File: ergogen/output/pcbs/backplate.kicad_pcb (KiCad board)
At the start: 2 copper layers, 133.8 x 91.7 mm, 5 parts

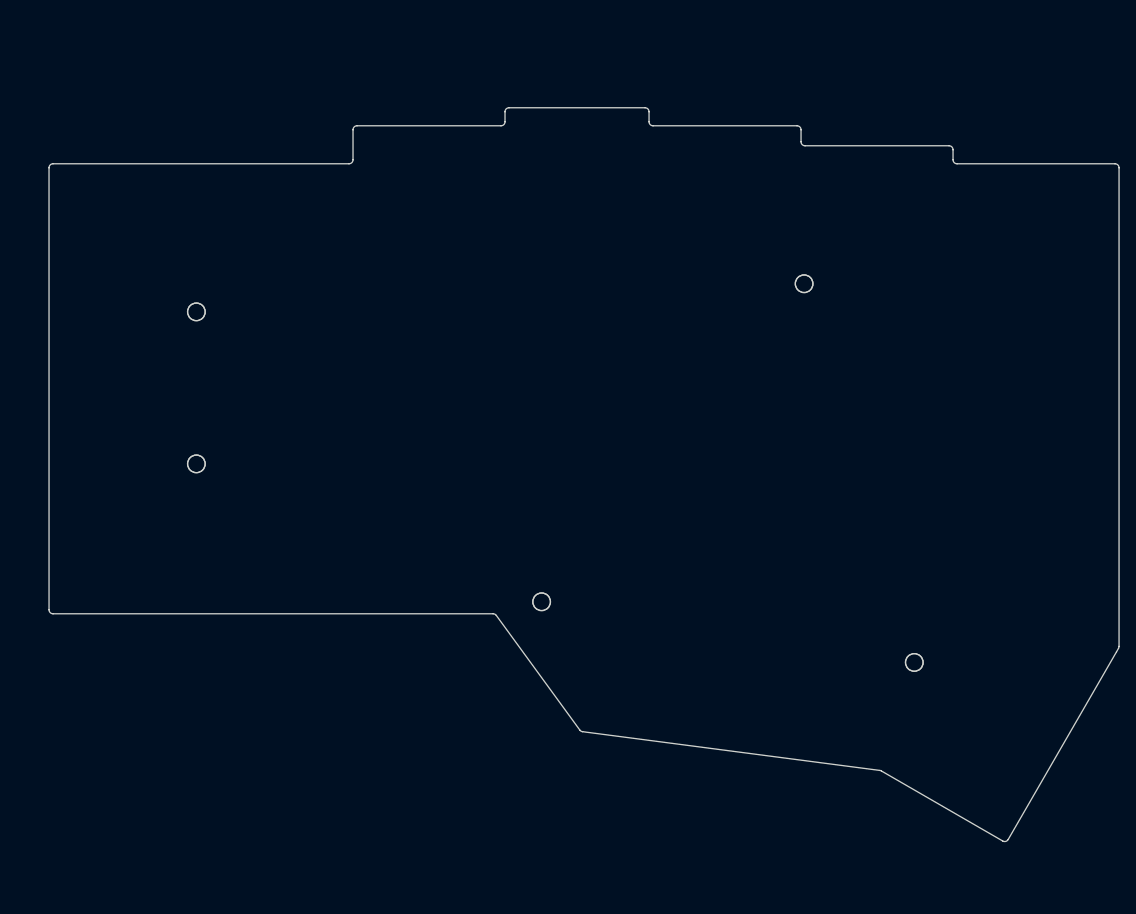
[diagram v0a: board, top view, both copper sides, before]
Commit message: Removed outer column
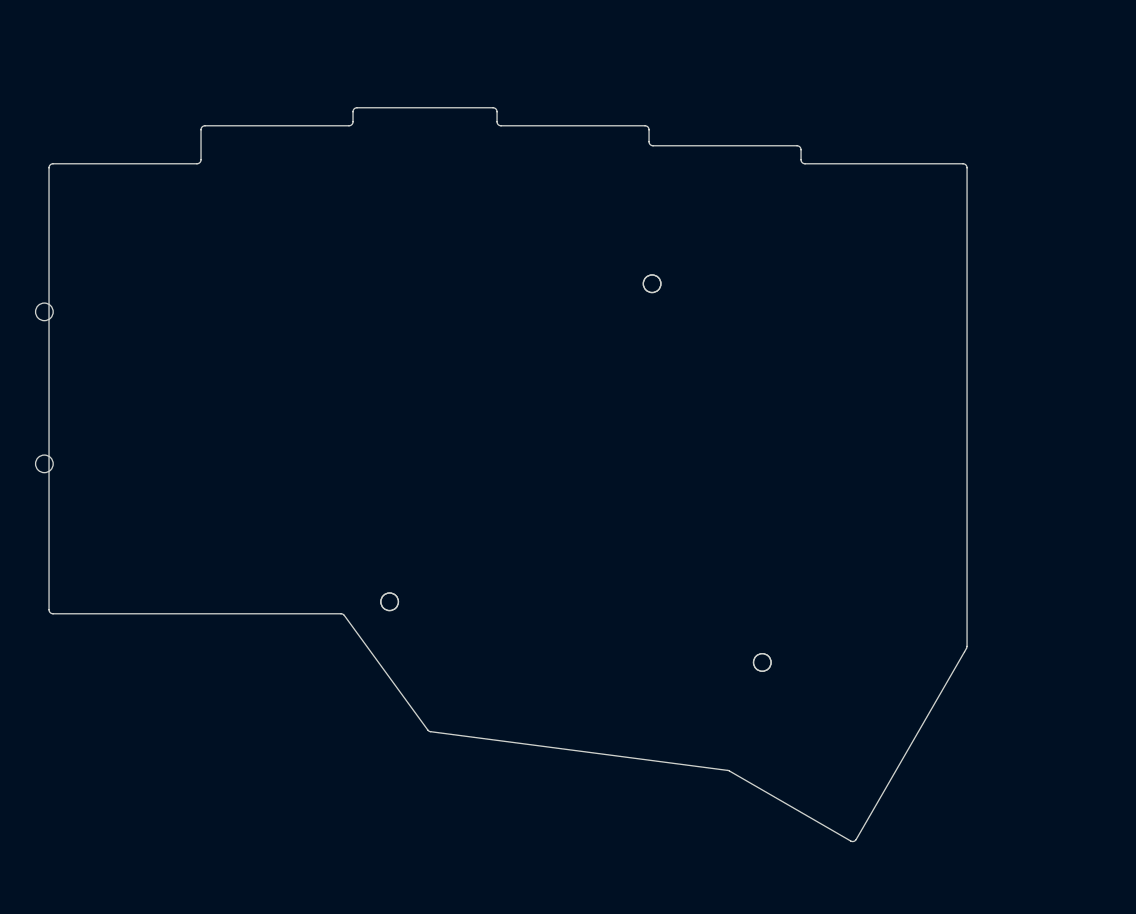
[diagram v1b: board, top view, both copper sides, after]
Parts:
- moved MH5 19.0 mm to (180.2, 115.3)
- moved MH1 19.0 mm to (90.5, 71.5)
- moved MH2 19.0 mm to (90.5, 90.5)
- moved MH3 19.0 mm to (166.5, 68.0)
- moved MH4 19.0 mm to (133.7, 107.7)
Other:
- board size 133.8 x 91.7 mm -> 114.8 x 91.7 mm

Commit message: Changed stagger to be like karia
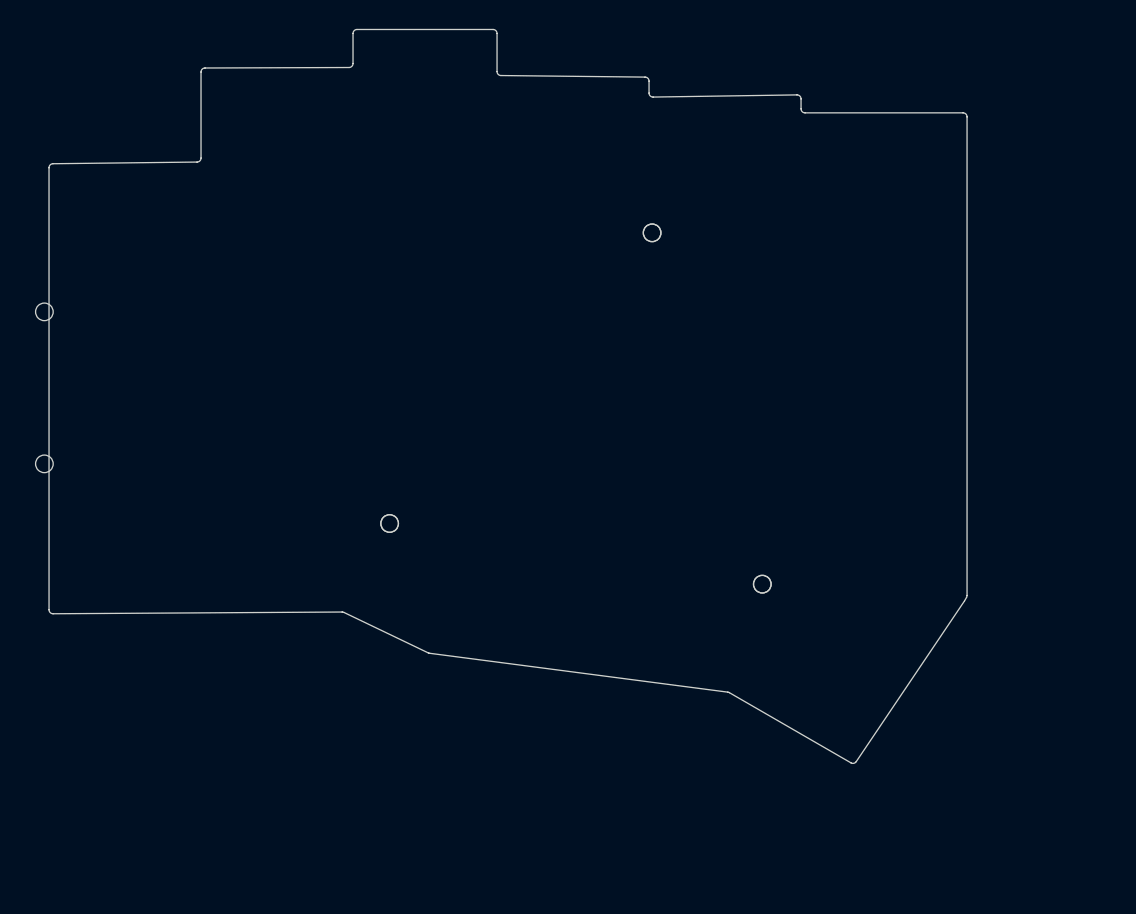
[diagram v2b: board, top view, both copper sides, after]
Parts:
- moved MH4 9.78 mm to (133.7, 98.0)
- moved MH5 9.78 mm to (180.2, 105.5)
- moved MH3 6.36 mm to (166.5, 61.6)
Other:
- outline, holes or cut-outs redrawn

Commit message: Added splay to pinky
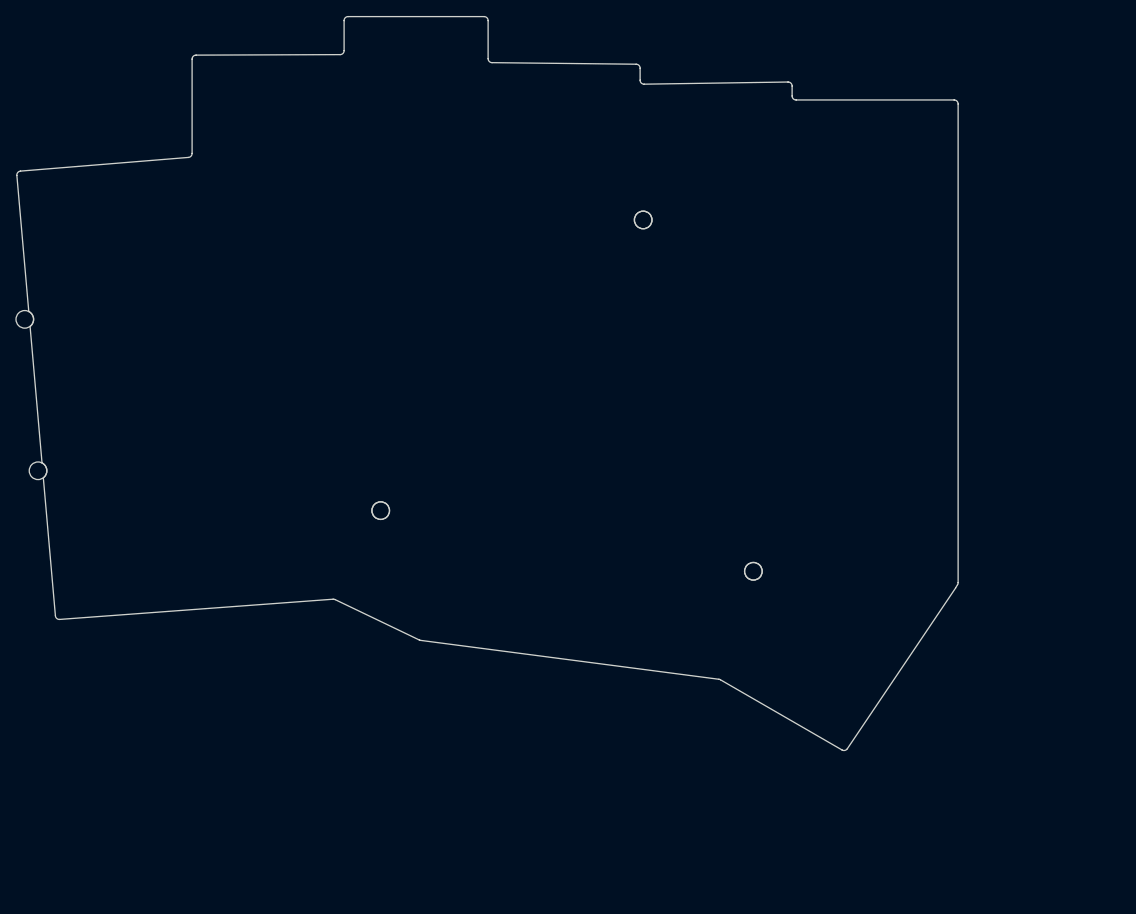
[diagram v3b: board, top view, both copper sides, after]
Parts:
- moved MH1 2.62 mm to (88.1, 72.4), turned to 5 degrees
- moved MH4 1.96 mm to (132.5, 96.3)
- moved MH5 1.96 mm to (179.1, 103.9)
- moved MH3 1.96 mm to (165.4, 60.0)
- moved MH2 1.17 mm to (89.7, 91.4), turned to 5 degrees
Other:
- board size 114.8 x 91.7 mm -> 117.7 x 91.7 mm

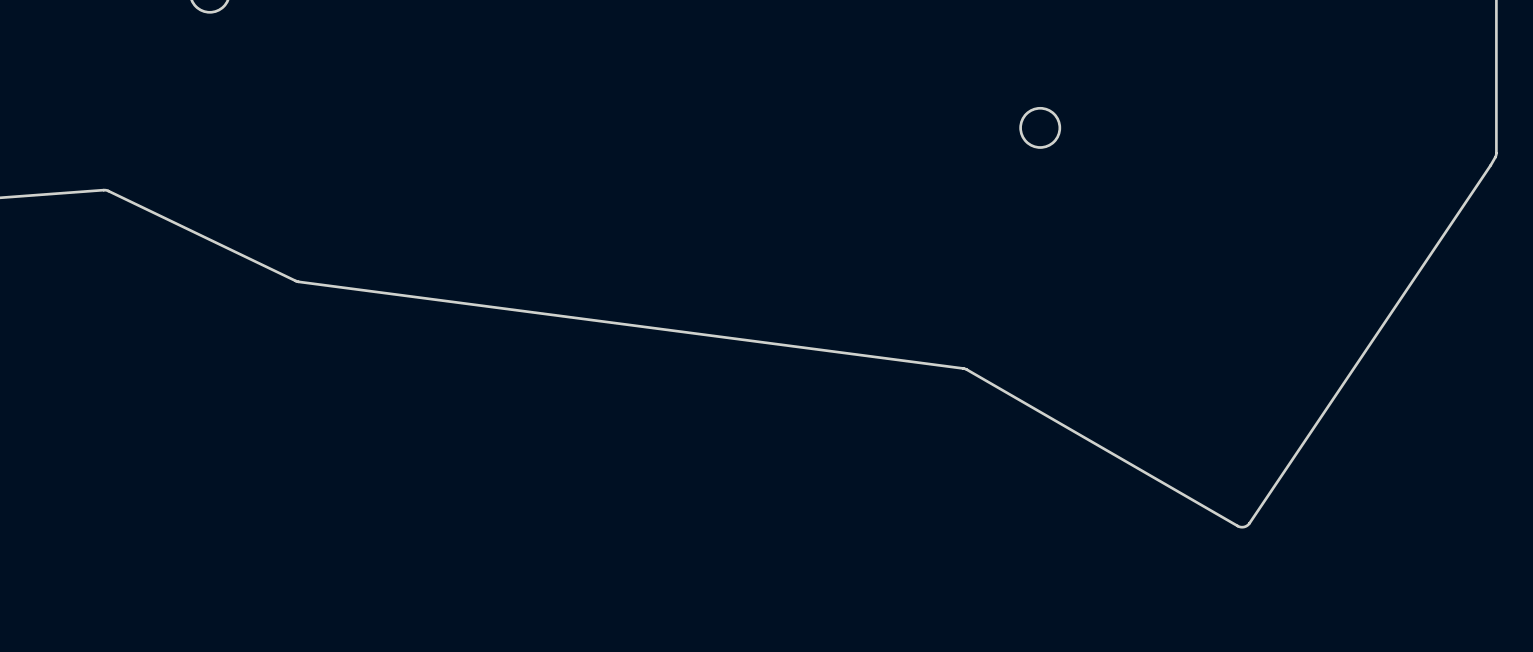
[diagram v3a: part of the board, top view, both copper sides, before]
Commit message: Changed thumb key back to 1u
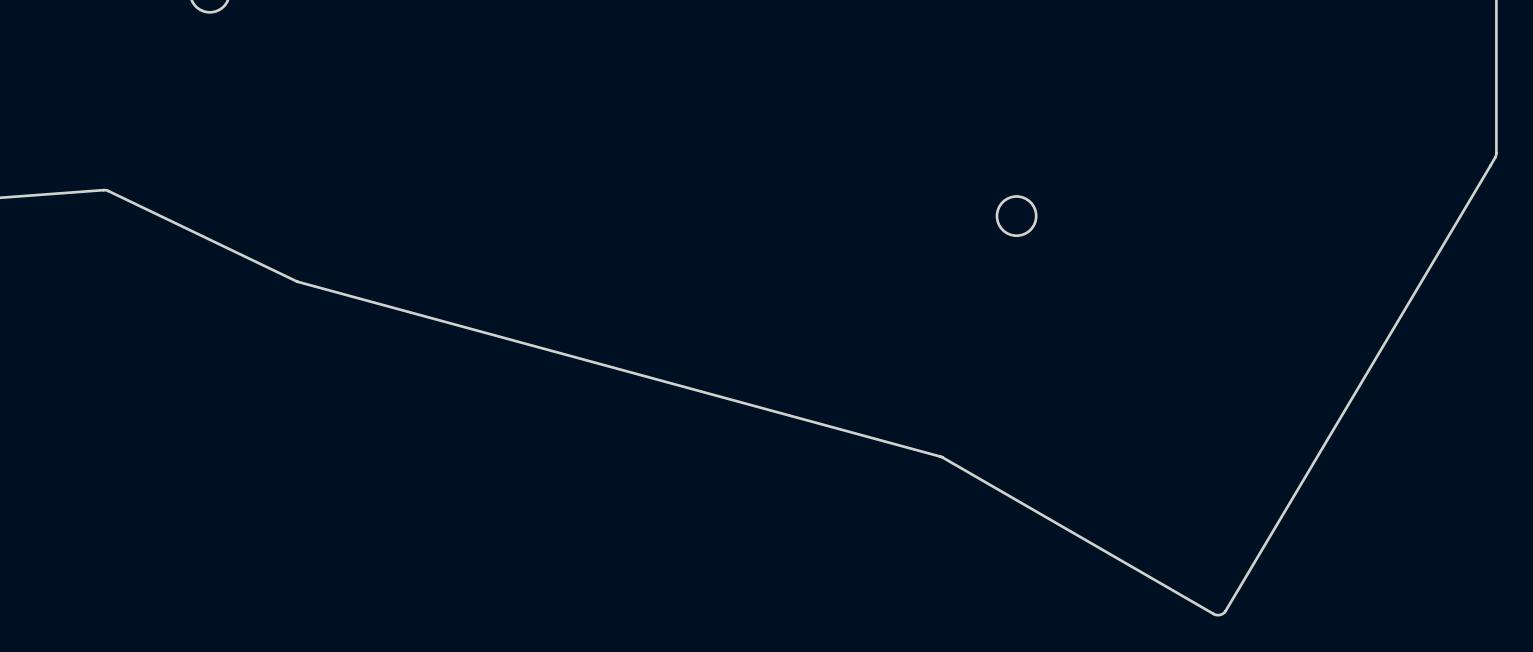
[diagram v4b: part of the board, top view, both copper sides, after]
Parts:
- moved MH5 5.12 mm to (177.8, 108.9)
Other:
- board size 117.7 x 91.7 mm -> 117.7 x 96.7 mm
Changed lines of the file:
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@@
   )
   (module "ceoloide:mounting_hole_npth" (layer F.Cu)
-      (at 179.1254966 103.9282479 60)
+      (at 177.7998255 108.87572 60)
       (fp_text reference "MH5" (at 0 2.55 60) (layer F.SilkS) hide (effects (font (size 1 1) (thickness 0.15))))
       (pad "" np_thru_hole circle (at 0 0 60) (size 2.2 2.2) (drill 2.2) (layers *.Cu *.Mask))
@@
 (gr_line (start 165.47394415076104 43.03997791277865) (end 183.45917122939375 42.77019950801905) (layer Edge.Cuts) (stroke (width 0.15) (type default)))
 (gr_line (start 183.96667038015485 43.26992130873259) (end 183.96722317371228 44.51481240004068) (layer Edge.Cuts) (stroke (width 0.15) (type default)))
-(gr_line (start 204.4024451 106.02118640000002) (end 190.86864454351888 126.1091037392597) (layer Edge.Cuts) (stroke (width 0.15) (type default)))
-(gr_line (start 190.20397584351886 126.26274233925967) (end 175.00808706223268 117.489391839137) (layer Edge.Cuts) (stroke (width 0.15) (type default)))
-(gr_line (start 174.82271206223268 117.42659853913699) (end 137.52391425873893 112.56494858875345) (layer Edge.Cuts) (stroke (width 0.15) (type default)))
-(gr_line (start 137.3721942392345 112.5199139793924) (end 126.84466306000907 107.46728833906016) (layer Edge.Cuts) (stroke (width 0.15) (type default)))
+(gr_line (start 204.4024451 106.02118640000002) (end 189.53461200661962 131.01926453205544) (layer Edge.Cuts) (stroke (width 0.15) (type default)))
+(gr_line (start 188.8548751066196 131.19668733205546) (end 173.65217521437296 122.41940443517656) (layer Edge.Cuts) (stroke (width 0.15) (type default)))
+(gr_line (start 173.533396814373 122.36994343517657) (end 137.48845271108377 112.56655937095499) (layer Edge.Cuts) (stroke (width 0.15) (type default)))
+(gr_line (start 137.40332929157933 112.53485706159397) (end 126.84466306000907 107.46728833906015) (layer Edge.Cuts) (stroke (width 0.15) (type default)))
 (gr_line (start 126.59146074050466 107.41942002969911) (end 92.41319770323031 109.94573156980263) (layer Edge.Cuts) (stroke (width 0.15) (type default)))
 (gr_line (start 184.46722317371226 45.01459040000001) (end 204.2174451 45.01459040000001) (layer Edge.Cuts) (stroke (width 0.15) (type default)))
@@
 (gr_arc (start 204.7174451 45.51459040000001) (mid 204.5709985 45.16103700000001) (end 204.2174451 45.01459040000001) (layer Edge.Cuts) (stroke (width 0.15) (type default)))
 (gr_arc (start 204.6504578 105.59161580612954) (mid 204.70040799999998 105.47102530612953) (end 204.7174451 105.34161580612954) (layer Edge.Cuts) (stroke (width 0.15) (type default)))
-(gr_arc (start 190.2039758435189 126.26274233925966) (mid 190.56658204351888 126.31688453925965) (end 190.86864454351888 126.10910373925965) (layer Edge.Cuts) (stroke (width 0.15) (type default)))
-(gr_arc (start 175.00808706223268 117.489391839137) (mid 174.91850206223268 117.448836139137) (end 174.82271206223268 117.426598539137) (layer Edge.Cuts) (stroke (width 0.15) (type default)))
-(gr_arc (start 137.37219425873894 112.51991398875344) (mid 137.44626115873893 112.54847228875344) (end 137.52391425873893 112.56494858875345) (layer Edge.Cuts) (stroke (width 0.15) (type default)))
+(gr_arc (start 188.8548751066196 131.1966873320555) (mid 189.2311528066196 131.2474658320555) (end 189.5346120066196 131.01926453205547) (layer Edge.Cuts) (stroke (width 0.15) (type default)))
+(gr_arc (start 173.65217521437296 122.41940443517656) (mid 173.59438361437296 122.39083733517657) (end 173.53339681437296 122.36994343517657) (layer Edge.Cuts) (stroke (width 0.15) (type default)))
+(gr_arc (start 137.40332931108378 112.534857070955) (mid 137.44516961108377 112.55264527095501) (end 137.48845271108377 112.566559370955) (layer Edge.Cuts) (stroke (width 0.15) (type default)))
 (gr_arc (start 126.84466304050464 107.46728832969912) (mid 126.72119864050464 107.42676222969911) (end 126.59146074050464 107.41942002969911) (layer Edge.Cuts) (stroke (width 0.15) (type default)))
 (gr_arc (start 91.8782446032303 109.49068746980264) (mid 92.0523782032303 109.82794416980263) (end 92.4131977032303 109.94573156980263) (layer Edge.Cuts) (stroke (width 0.15) (type default)))
@@
 (gr_circle (center 165.35244509999998 60.01059040000001) (end 166.45244509999998 60.01059040000001) (layer Edge.Cuts) (stroke (width 0.15) (type default)) (fill none))
 (gr_circle (center 132.541445 96.3445903) (end 133.641445 96.3445903) (layer Edge.Cuts) (stroke (width 0.15) (type default)) (fill none))
-(gr_circle (center 179.1254966 103.9282479) (end 180.22549659999999 103.9282479) (layer Edge.Cuts) (stroke (width 0.15) (type default)) (fill none))
+(gr_circle (center 177.7998255 108.87572) (end 178.8998255 108.87572) (layer Edge.Cuts) (stroke (width 0.15) (type default)) (fill none))
 )
